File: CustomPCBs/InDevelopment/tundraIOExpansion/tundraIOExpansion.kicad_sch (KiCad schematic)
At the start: 54 parts, among them J1 Conn_01x25, J2 Conn_ARM_SWD_TagConnect_TC203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, J3 Conn_ARM_SWD_TagConnect_TC203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, U1 RP2040, U2 MX25L3233FM2, U4 MX25L3233FM2, U5 RP2040, Y1 12.000MHz, Y2 12.000MHz, Y3 32.768kHz

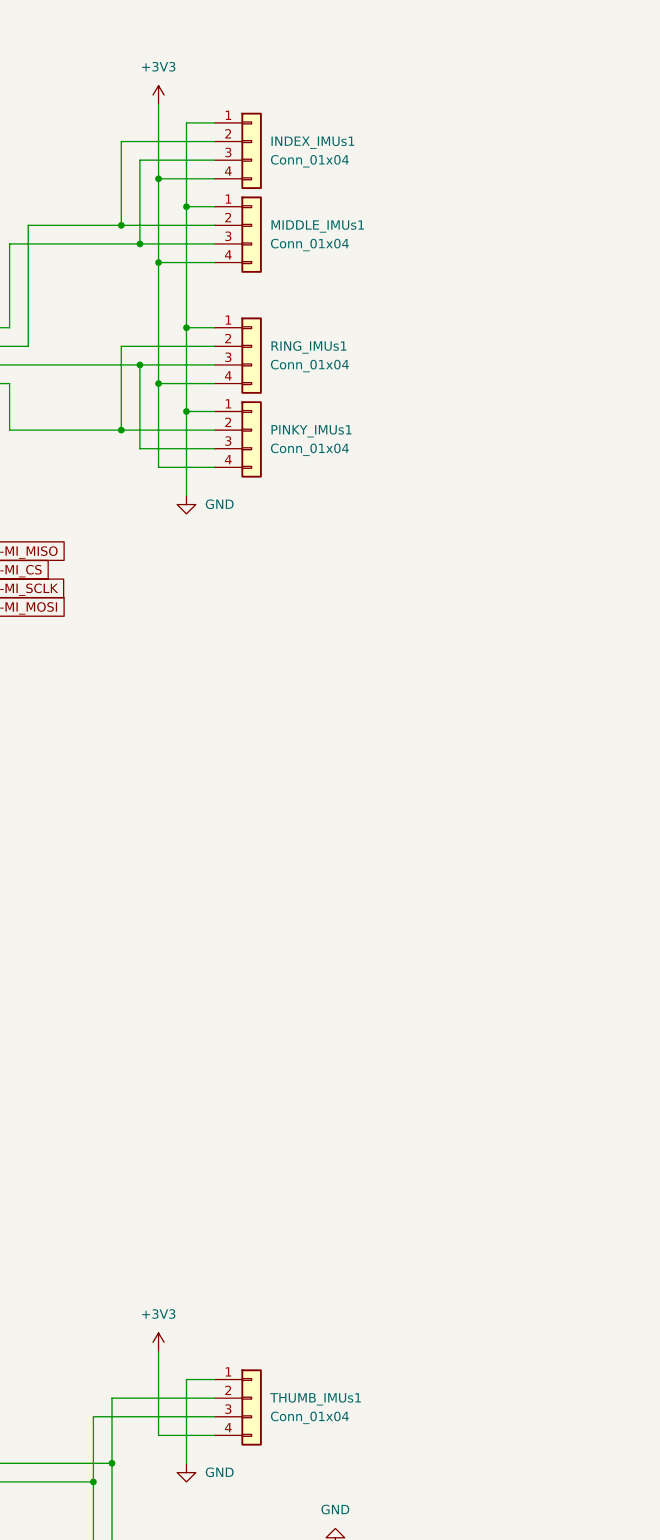
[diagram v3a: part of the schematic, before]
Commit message: Component placement complete
Will still experiment with inputs first so I know what kind of
connectors will be needed to get whatever buttons or joysticks may be
inplemented. Only after that's done will the routing of the tracks
start.
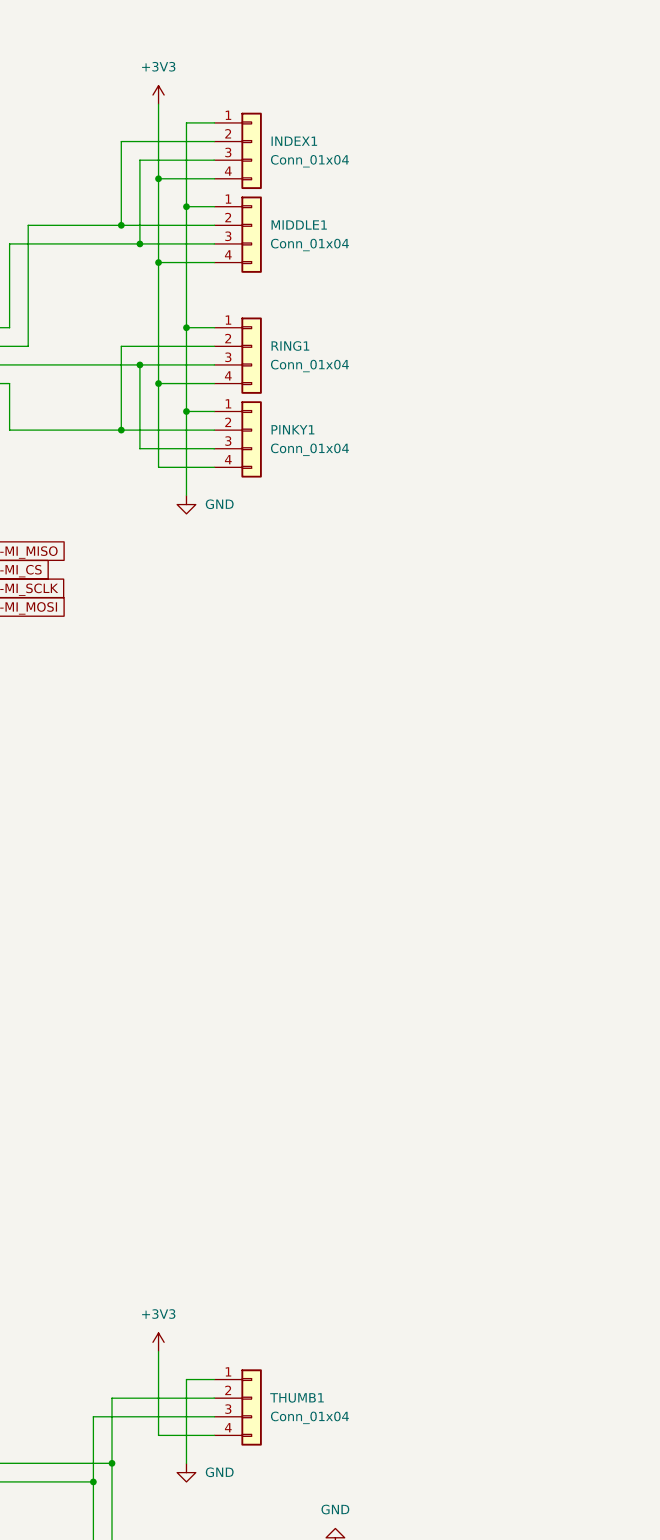
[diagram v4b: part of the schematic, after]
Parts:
- renumbered INDEX_IMUs1 to INDEX1, MIDDLE_IMUs1 to MIDDLE1, PINKY_IMUs1 to PINKY1, RING_IMUs1 to RING1, THUMB_IMUs1 to THUMB1
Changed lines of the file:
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@@
   (symbol (lib_id "Connector_Generic:Conn_01x04") (at 242.57 82.55 0) (unit 1)
     (in_bom yes) (on_board yes) (dnp no) (fields_autoplaced)
-    (property "Reference" "PINKY_IMUs1" (at 245.11 82.55 0)
+    (property "Reference" "PINKY1" (at 245.11 82.55 0)
       (effects (font (size 1.27 1.27)) (justify left))
     )
@@
       (project "tundraIOExpansion"
         (path "/6bc6d498-c151-42bc-9dad-57407f39c6cd"
-          (reference "PINKY_IMUs1") (unit 1)
+          (reference "PINKY1") (unit 1)
         )
       )
@@
   (symbol (lib_id "Connector_Generic:Conn_01x04") (at 242.57 214.63 0) (unit 1)
     (in_bom yes) (on_board yes) (dnp no) (fields_autoplaced)
-    (property "Reference" "THUMB_IMUs1" (at 245.11 214.63 0)
+    (property "Reference" "THUMB1" (at 245.11 214.63 0)
       (effects (font (size 1.27 1.27)) (justify left))
     )
@@
       (project "tundraIOExpansion"
         (path "/6bc6d498-c151-42bc-9dad-57407f39c6cd"
-          (reference "THUMB_IMUs1") (unit 1)
+          (reference "THUMB1") (unit 1)
         )
       )
@@
   (symbol (lib_id "Connector_Generic:Conn_01x04") (at 242.57 71.12 0) (unit 1)
     (in_bom yes) (on_board yes) (dnp no) (fields_autoplaced)
-    (property "Reference" "RING_IMUs1" (at 245.11 71.12 0)
+    (property "Reference" "RING1" (at 245.11 71.12 0)
       (effects (font (size 1.27 1.27)) (justify left))
     )
@@
       (project "tundraIOExpansion"
         (path "/6bc6d498-c151-42bc-9dad-57407f39c6cd"
-          (reference "RING_IMUs1") (unit 1)
+          (reference "RING1") (unit 1)
         )
       )
@@
   (symbol (lib_id "Connector_Generic:Conn_01x04") (at 242.57 43.18 0) (unit 1)
     (in_bom yes) (on_board yes) (dnp no) (fields_autoplaced)
-    (property "Reference" "INDEX_IMUs1" (at 245.11 43.18 0)
+    (property "Reference" "INDEX1" (at 245.11 43.18 0)
       (effects (font (size 1.27 1.27)) (justify left))
     )
@@
       (project "tundraIOExpansion"
         (path "/6bc6d498-c151-42bc-9dad-57407f39c6cd"
-          (reference "INDEX_IMUs1") (unit 1)
+          (reference "INDEX1") (unit 1)
         )
       )
@@
   (symbol (lib_id "Connector_Generic:Conn_01x04") (at 242.57 54.61 0) (unit 1)
     (in_bom yes) (on_board yes) (dnp no) (fields_autoplaced)
-    (property "Reference" "MIDDLE_IMUs1" (at 245.11 54.61 0)
+    (property "Reference" "MIDDLE1" (at 245.11 54.61 0)
       (effects (font (size 1.27 1.27)) (justify left))
     )
@@
       (project "tundraIOExpansion"
         (path "/6bc6d498-c151-42bc-9dad-57407f39c6cd"
-          (reference "MIDDLE_IMUs1") (unit 1)
-        )
-      )
+          (reference "MIDDLE1") (unit 1)
+        )
+      )

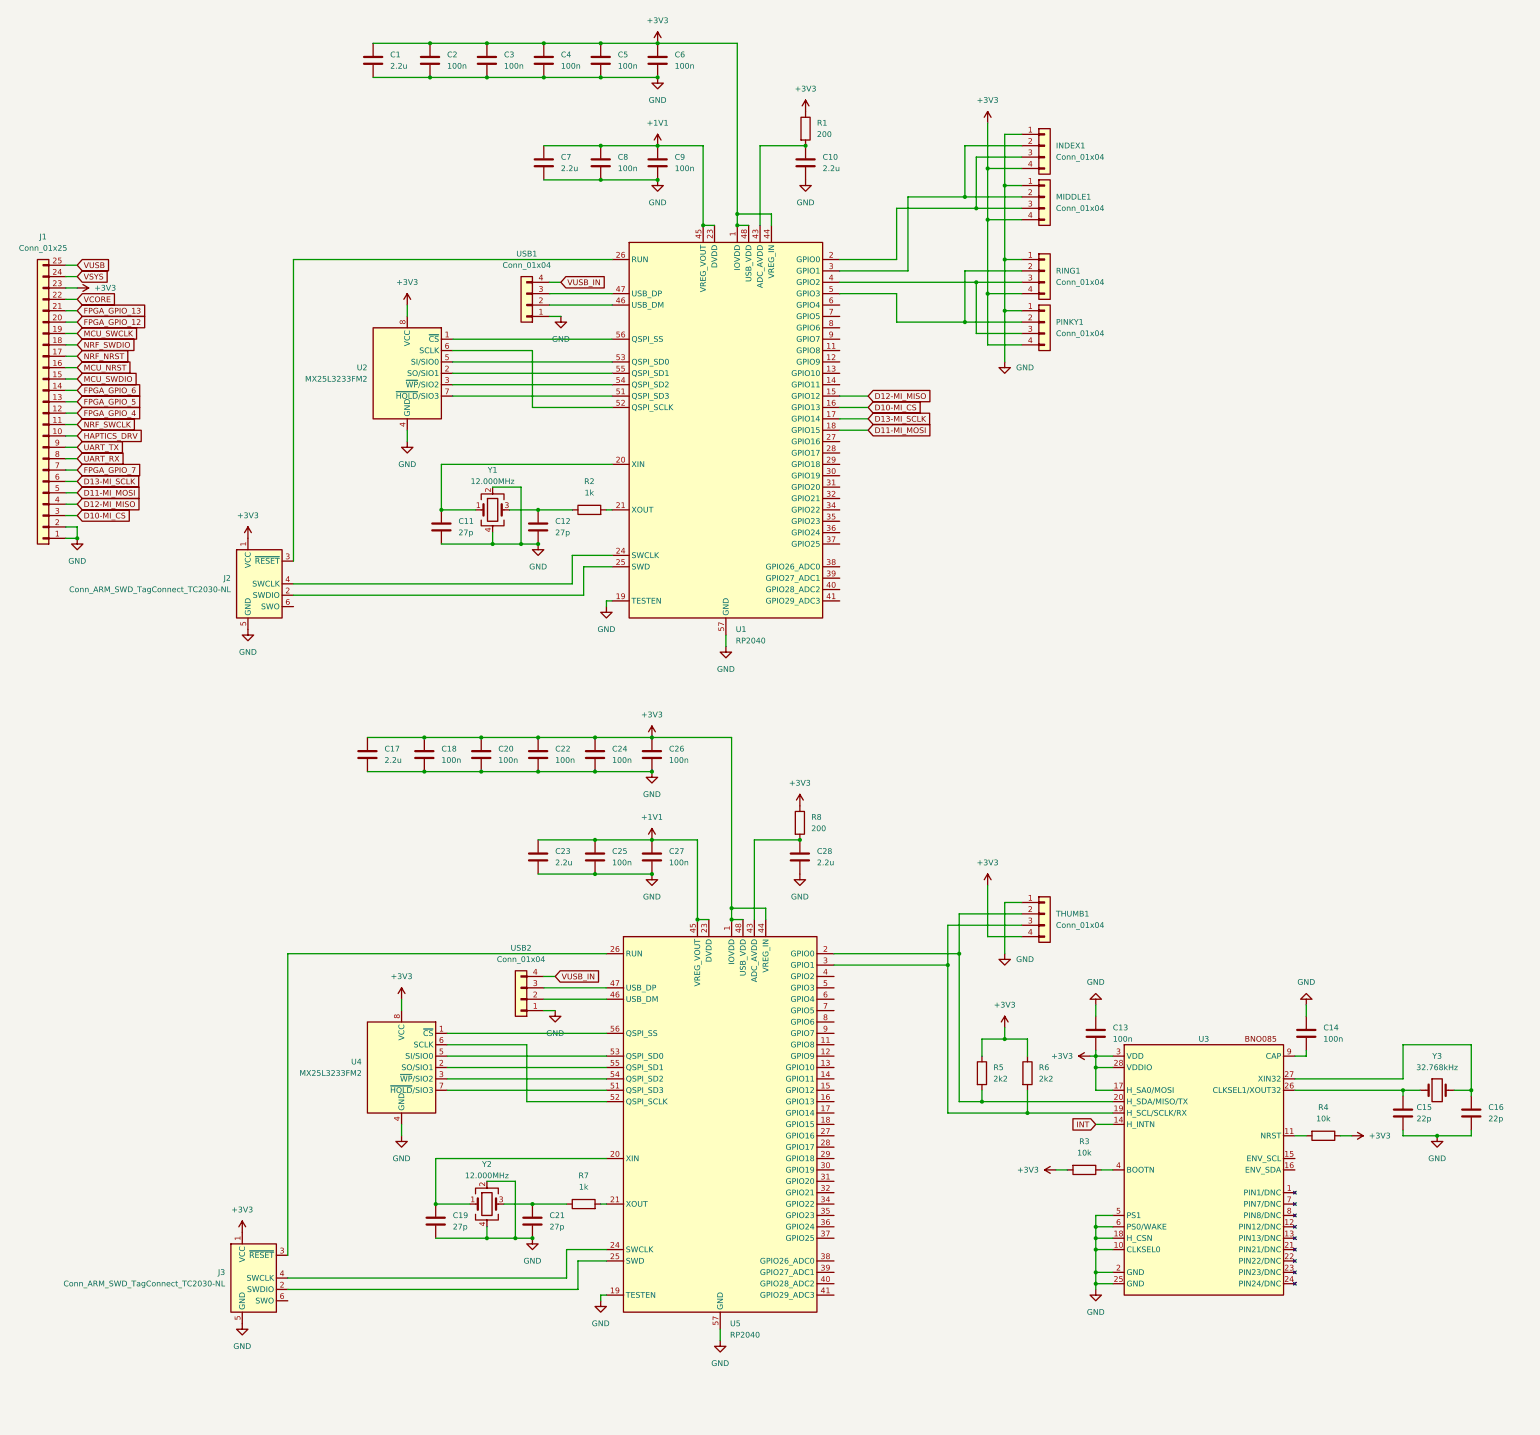
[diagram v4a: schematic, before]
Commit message: Adding auxiliary connectors for mixed inputs
I am still not sure what input types I will have, but I am preparing the
board to be flexible, exposing 8 GPIOs, 4 of which are analog to digital
converters.

I have also started to design the hardware interface with a second board
that can be placed below the main one, to add two rp2040 to the project
if needed.
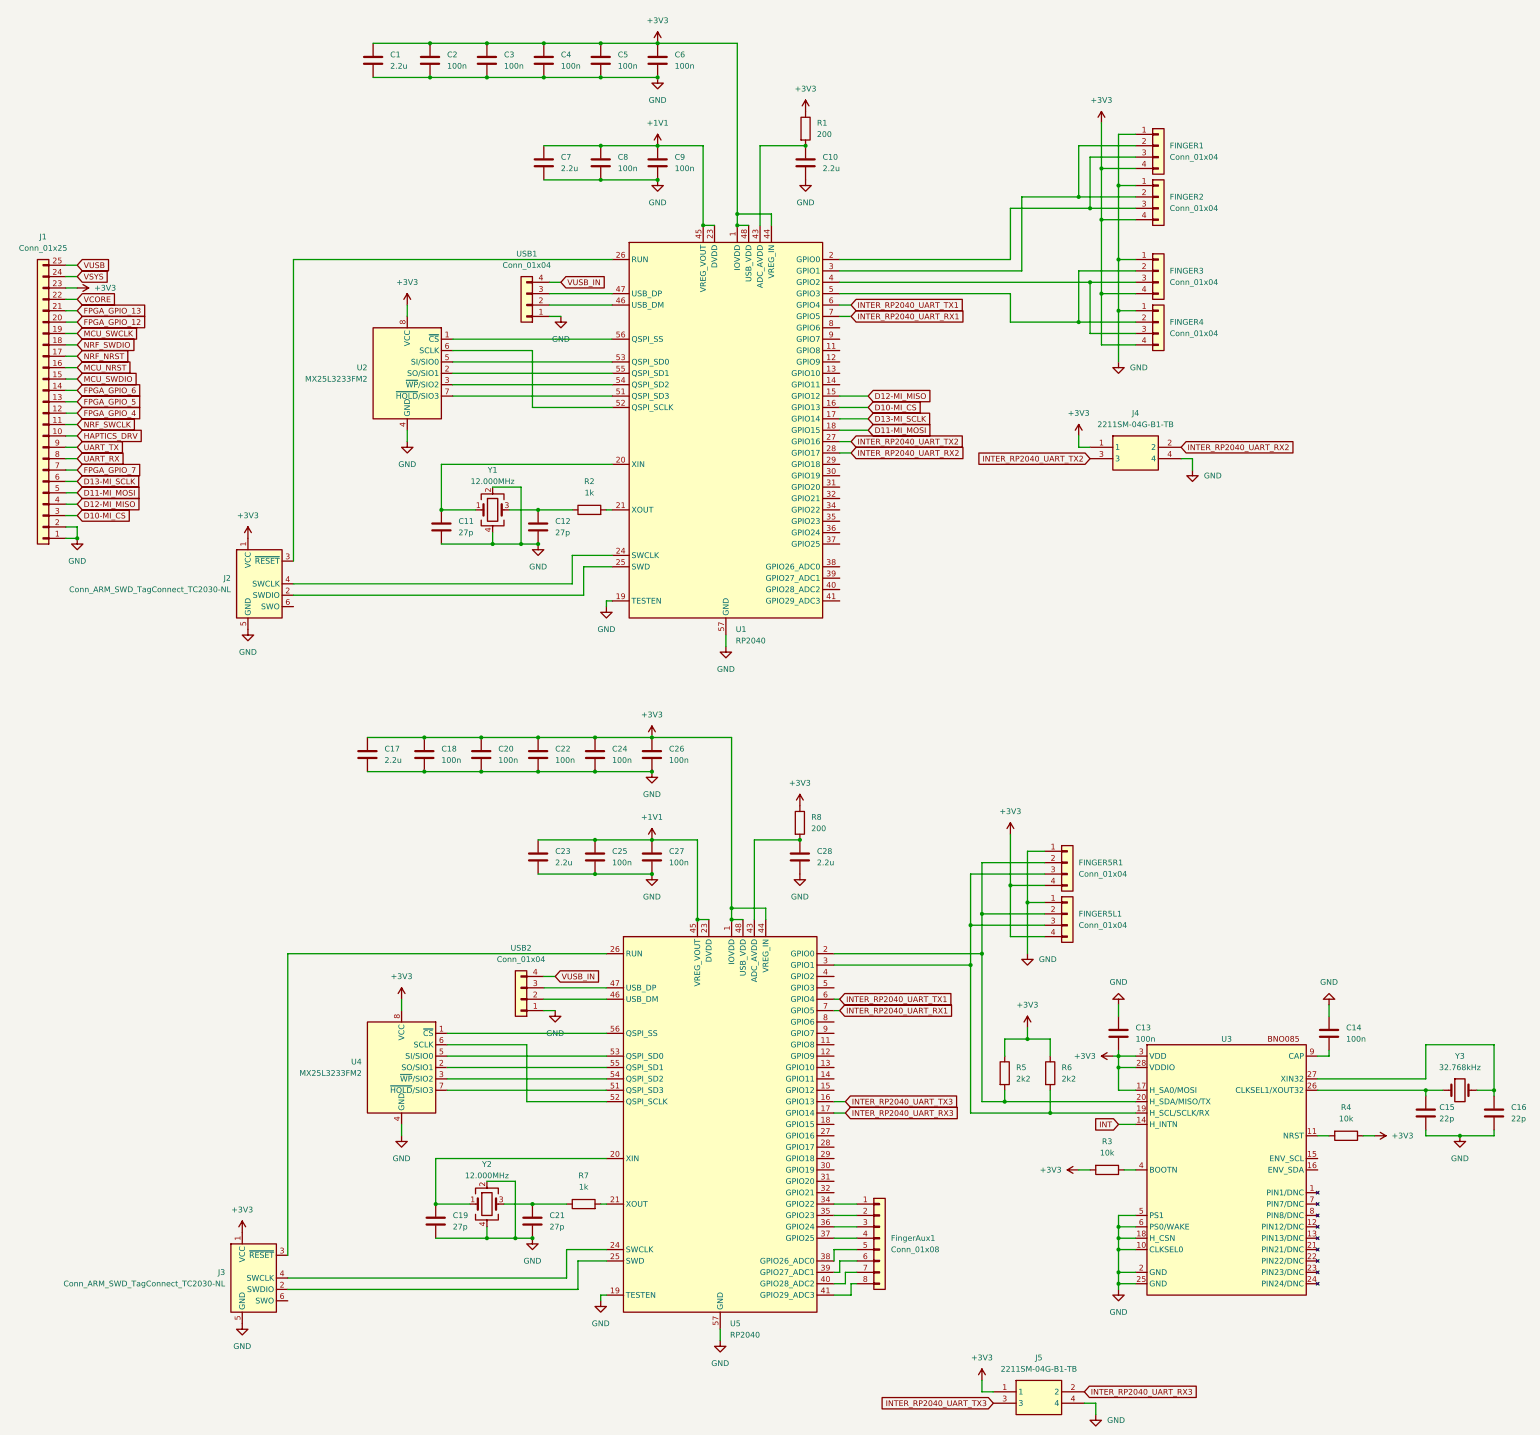
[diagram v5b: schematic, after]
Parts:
- removed MIDDLE1, PINKY1, RING1, THUMB1: Conn_01x04, Connector_JST:JST_SH_SM04B-SRSS-TB_1x04-1MP_P1.00mm_Horizontal, symbol Connector_Generic:Conn_01x04
- added FINGER2, FINGER3, FINGER4, FINGER5L1, FINGER5R1: Conn_01x04, Connector_JST:JST_SH_SM04B-SRSS-TB_1x04-1MP_P1.00mm_Horizontal, symbol Connector_Generic:Conn_01x04
- added FingerAux1: Conn_01x08, Connector_JST:JST_SH_SM08B-SRSS-TB_1x08-1MP_P1.00mm_Horizontal, symbol Connector_Generic:Conn_01x08
- added J4, J5: 2211SM-04G-B1-TB, Connector_Harting:Harting_har-flexicon_14110413001xxx_1x04-MP_P2.54mm_Vertical, symbol 2211SM-04G-B1-TB:2211SM-04G-B1-TB
- renumbered INDEX1 to FINGER1
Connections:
- net +3V3: now also FINGER2.4 (Pin_4), FINGER3.4 (Pin_4), FINGER4.4 (Pin_4), FINGER5L1.4 (Pin_4), FINGER5R1.4 (Pin_4), J4.1, J5.1
- net GND: now also FINGER2.1 (Pin_1), FINGER3.1 (Pin_1), FINGER4.1 (Pin_1), FINGER5L1.1 (Pin_1), FINGER5R1.1 (Pin_1), J4.4, J5.4
- net at R5.2, U3.20 (H_SDA/MISO/TX), U5.2 (GPIO0): now also FINGER5L1.2 (Pin_2), FINGER5R1.2 (Pin_2)
- net at FINGER1.3 (Pin_3), U1.2 (GPIO0): now also FINGER2.3 (Pin_3)
- net INTER_RP2040_UART_TX2: now reaches U1.27 (GPIO16)
- net INTER_RP2040_UART_TX2: now also J4.3
- net INTER_RP2040_UART_RX2: now reaches U1.28 (GPIO17)
- net INTER_RP2040_UART_RX2: now also J4.2
- net at FINGER1.2 (Pin_2), U1.3 (GPIO1): now also FINGER2.2 (Pin_2)
- net at U1.4 (GPIO2): now also FINGER3.3 (Pin_3), FINGER4.3 (Pin_3)
- net at U1.5 (GPIO3): now also FINGER3.2 (Pin_2), FINGER4.2 (Pin_2)
- net INTER_RP2040_UART_TX1: now reaches U1.6 (GPIO4)
- net INTER_RP2040_UART_TX1: now also U5.6 (GPIO4)
- net INTER_RP2040_UART_RX1: now reaches U1.7 (GPIO5)
- net INTER_RP2040_UART_RX1: now also U5.7 (GPIO5)
- net at R6.2, U3.19 (H_SCL/SCLK/RX), U5.3 (GPIO1): now also FINGER5L1.3 (Pin_3), FINGER5R1.3 (Pin_3)
- net INTER_RP2040_UART_TX3: now reaches U5.16 (GPIO13)
- net INTER_RP2040_UART_TX3: now also J5.3
- net INTER_RP2040_UART_RX3: now reaches U5.17 (GPIO14)
- net INTER_RP2040_UART_RX3: now also J5.2
- net at U5.34 (GPIO22): now also FingerAux1.1 (Pin_1)
- net at U5.35 (GPIO23): now also FingerAux1.2 (Pin_2)
- net at U5.36 (GPIO24): now also FingerAux1.3 (Pin_3)
- net at U5.37 (GPIO25): now also FingerAux1.4 (Pin_4)
- net at U5.38 (GPIO26_ADC0): now also FingerAux1.5 (Pin_5)
- net at U5.39 (GPIO27_ADC1): now also FingerAux1.6 (Pin_6)
- net at U5.40 (GPIO28_ADC2): now also FingerAux1.7 (Pin_7)
- net at U5.41 (GPIO29_ADC3): now also FingerAux1.8 (Pin_8)
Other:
- moved on the sheet: C13, C14, C15, C16, FINGER1, R3, R4, R5, R6, U3, Y3
